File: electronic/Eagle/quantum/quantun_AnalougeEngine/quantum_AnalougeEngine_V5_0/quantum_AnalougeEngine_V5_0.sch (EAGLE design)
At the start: 204 parts, among them IC1 OP275, IC10 STM32F767ZIT6, IC11 AD7606BSTZ, IC2 DAC084S085CIMM_NOPB, IC3 DAC084S085CIMM_NOPB, IC4 OP275, IC5 OP275, IC6 LAN8742A-CZ-TR, IC7 TL072, IC8 OP275, IC9 TL072, J1 GWLEX-SMT-S988G_Y, K1 K1, K2 K2, K3 K3, K4 K4, K5 K5, K6 K6, K7 K7, K8 K8, T1 H1102NL, U12 ULN2003, U2 7812, U4 THAT1240, U6 THAT1240, U7 THAT1240, U8 THAT1240

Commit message: Continued on "AnlougeEngine_V_5_0" - Changed little timing in ADC read. Changed left/right send to FrontDisplay
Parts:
- removed CON1, CON2, CON3: (no value), electro_mechanical:PIN_HEADER_RIBBON_10_PIN_SMD
- removed R15, R16, R17, R18, R19, R20, R21, R22, R23, R24, R25, R26, R27: 10k, C_Sager_Bibliothek:RESISTOR
- added C44: 100nF, C_Sager_Bibliothek:CAPACITOR"
- added J2, J3, J4: 90814-0204, electro_mechanical:90814-0204
- added LED10, LED11, LED9: LED_BLUE_SMD, C_Sager_Bibliothek:LED_BLUE_SMD
- added R78: 10 k, C_Sager_Bibliothek:RESISTOR
- C41: value (none) -> 100 nF
- R13, R5: value 10k -> 680R; SPICEPREFIX R -> (none)
- R6: value 10k -> 680R
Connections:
- removed net N$10: IC11.V3, R16.2, R17.2
- removed net N$20: IC11.V5, R19.2, R24.2
- removed net N$35: IC11.V7, R21.2, R26.2
- removed net N$36: IC11.V8, R22.2, R27.2
- removed net N$46: R21.1
- new net DEBUG1: IC10.PF9
- new net DEBUG2: IC10.PD1
- new net LD1: IC10.PB0, LED9.+
- new net LD2: IC10.PB7, LED10.+
- new net LD3: IC10.PB14, LED11.+
- new net N$100: IC10.PC1
- new net N$101: IC10.PC2
- new net N$103: IC10.VDD_2
- new net N$104: IC10.VSSA
- new net N$105: IC10.VREF+
- new net N$106: IC10.VDDA
- new net N$107: IC10.PA0
- new net N$108: IC10.PA1
- new net N$109: IC10.PA2
- new net N$110: IC10.PA3
- new net N$111: IC10.VSS_2
- new net N$112: IC10.VDD_3
- new net N$115: IC10.PA6
- new net N$116: IC10.PA7
- new net N$117: IC10.PC4
- new net N$118: IC10.PC5
- new net N$120: IC10.PB1
- new net N$121: IC10.PB2
- new net N$122: IC10.PF11
- new net N$123: IC10.PF12
- new net N$124: IC10.VSS_3
- new net N$125: IC10.VDD_4
- new net N$126: IC10.PF13
- new net N$127: IC10.PF14
- new net N$128: IC10.PF15
- new net N$134: IC10.VSS_4
- new net N$135: IC10.VDD_5
- new net N$143: IC10.PB11
- new net N$144: IC10.VCAP_1
- new net N$145: IC10.VDD_6
- new net N$146: IC10.VDD_8
- new net N$147: IC10.VSS_7
- new net N$148: IC10.VCAP_2
- new net N$150: IC10.PA12
- new net N$151: IC10.PA11
- new net N$152: IC10.PA10
- new net N$153: IC10.PA9
- new net N$154: IC10.PA8
- new net N$159: IC10.VDDUSB
- new net N$160: IC10.VSS_6
- new net N$161: IC10.PG8
- new net N$162: IC10.PG7
- new net N$163: IC10.PG6
- new net N$164: IC10.PG5
- new net N$165: IC10.PG4
- new net N$168: IC10.PD15
- new net N$169: IC10.PD14
- new net N$170: IC10.VDD_7
- new net N$171: IC10.VSS_5
- new net N$172: IC10.PD13
- new net N$173: IC10.PD12
- new net N$174: IC10.PD11
- new net N$175: IC10.PD10
- new net N$178: IC10.PB15
- new net N$180: IC10.PB13
- new net N$181: IC10.PB12
- new net N$182: IC10.VDD_10
- new net N$183: IC10.PDR_ON
- new net N$186: IC10.PB9
- new net N$187: IC10.PB8
- new net N$188: IC10.BOOT0, R78.1
- new net N$190: IC10.PB6
- new net N$193: IC10.PB3
- new net N$195: IC10.VDD_9
- new net N$196: IC10.VSS_9
- new net N$197: IC10.PG14
- new net N$198: IC10.PG13
- new net N$200: IC10.PG11
- new net N$205: IC10.VDDSDMMC
- new net N$206: IC10.VSS_8
- new net N$207: IC10.PD5
- new net N$208: IC10.PD4
- new net N$209: IC10.PD3
- new net N$212: IC10.PD0
- new net N$216: IC10.PA15
- new net N$69: IC10.VBAT
- new net N$70: IC10.PC13
- new net N$76: IC10.PC14
- new net N$82: IC10.PC15
- new net N$83: IC10.PF0
- new net N$84: IC10.PF1
- new net N$85: IC10.PF2
- new net N$86: IC10.PF3
- new net N$87: IC10.PF4
- new net N$88: IC10.PF5
- new net N$89: IC10.VSS_1
- new net N$90: IC10.VDD_1
- new net N$91: IC10.PF6
- new net N$92: IC10.PF7
- new net N$93: IC10.PF8
- new net N$95: IC10.PF10
- new net N$96: IC10.PH0
- new net N$97: IC10.PH1
- new net N$99: IC10.PC0
- new net NRST: C44.2, IC10.NRST, J4.2, S1.3, S1.4
- new net SWCLK: IC10.PA14, J4.1
- new net SWDIO: IC10.PA13, J4.3
- new net USART3_RX: IC10.PD8
- new net USART3_TX: IC10.PD9
- new net USART6_RX: IC10.PC6
- new net USART6_TX: IC10.PC7
- net AGND: now also C44.1, J4.4, R13.1, R5.1, R78.2, S1.1, S1.2; no longer R15.1, R16.1, R23.1, R24.1, R25.1, R26.1, R27.1
- net BUSY: now also IC10.PG3
- net CS: now also IC10.PD7
- net CS_DAC1: now also IC10.PB4
- net CS_DAC2: now also IC10.PB5
- net CV_A_B: now also IC10.PC12
- net DAC_OUT1: now also IC10.PA4
- net DAC_OUT2: now also IC10.PA5
- net DB0: now also IC10.PE0
- net DB1: now also IC10.PE1
- net DB10: now also IC10.PE10
- net DB11: now also IC10.PE11
- net DB12: now also IC10.PE12
- net DB13: now also IC10.PE13
- net DB14: now also IC10.PE14
- net DB15: now also IC10.PE15
- net DB2: now also IC10.PE2
- net DB3: now also IC10.PE3
- net DB4: now also IC10.PE4
- net DB5: now also IC10.PE5
- net DB6: now also IC10.PE6
- net DB7: now also IC10.PE7
- net DB8: now also IC10.PE8
- net DB9: now also IC10.PE9
- net DIN_DAC: now also IC10.PC3
- net FRST: now also IC10.PD6
- net L/M_IN(VCA1_IN): now also IC11.V1; no longer R5.1
- net L/M_OUT(OUT_STAGE_LEFT): now also IC11.V5; no longer R19.1
- net L/M_OUT(VCA1_OUT): now also IC11.V3; no longer R17.1
- net N$12: now also LED10.-, R6.2; no longer IC11.V4, R18.2, R23.2
- net N$34: now also LED11.-, R13.2; no longer IC11.V6, R20.2, R25.2
- net N$4: now also IC11.V7; no longer IC11.V1, R5.2, R6.2
- net N$47: now also IC11.V8; no longer R22.1
- net N$6: now also LED9.-, R5.2; no longer IC11.V2, R13.2, R15.2
- net OS0: now also IC10.PC8
- net OS1: now also IC10.PC9
- net OS2: now also IC10.PC10
- net R/S_IN(VCA2_IN): now also IC11.V2; no longer R13.1
- net R/S_OUT(OUT_STAGE_RIGHT): now also IC11.V6; no longer R20.1
- net R/S_OUT(VCA2_OUT): now also IC11.V4; no longer R18.1
- net RANGE: now also IC10.PC11
- net RD: now also IC10.PD2
- net RELAIS1: now also IC10.PG1
- net RELAIS2: now also IC10.PG0
- net RELAIS3: now also IC10.PG15
- net RELAIS4: now also IC10.PG10
- net RELAIS5: now also IC10.PG12
- net RELAIS6: now also IC10.PG9
- net RESET: now also IC10.PG2
- net SCLK_DAC: now also IC10.PB10
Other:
- note added: "debug LEDs"
- note added: "operational voltage"
- note added: "prg.adapter"
- note added: "reset switch"

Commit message: progess on Analouge Engine V_5_0
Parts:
- removed C69: 0.33 uF, C_Sager_Bibliothek:CAPACITOR"
- removed C70: 100 nF, C_Sager_Bibliothek:CAPACITOR"
- removed J2, J3, J4: 90814-0204, electro_mechanical:90814-0204
- removed R77: 0R, C_Sager_Bibliothek:RESISTOR
- removed TP03, TP05, TP06: TPTHT, C_Sager_Bibliothek:TPTHT
- removed U2: 7812, C_Sager_Bibliothek:78
- added ANALOGVOLT, DIG_VOLT, PROG.: 90814-0204, electro_mechanical:90814-0204
- added DEBUG1, DEBUG2, TP04: TPTHT, C_Sager_Bibliothek:TPTHT
- added IC12: ESDA6V1BC6, NUCLEO_parts:ESDA6V1BC6
- added R15, R16, R17: 0R, C_Sager_Bibliothek:RESISTOR
- added R18, R19: 10 k, C_Sager_Bibliothek:RESISTOR
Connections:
- net N$100 renamed RMII_MDC
- net N$108 renamed RMII_REF_CLK
- net N$109 renamed RMII_MDIO
- net N$116 renamed RMSII_CRS_DV
- net N$117 renamed RMII_RXD0
- net N$118 renamed RMII_RXD1
- net N$15 renamed NEGATIVE_OUT(L/M)
- net N$152 renamed USB_ID
- net N$17 renamed POSITIVE_OUT(L/M)
- net N$180 renamed RMII_TXD1
- net N$188 renamed BOOT0
- net N$198 renamed RMII_TXD0
- net N$200 renamed RMII_TX_EN
- net N$21 renamed POSITIVE_IN(R/S)
- net N$22 renamed NEGATIVE_IN(R/S)
- net N$23 renamed POSITIVE_OUT(R/S)
- net N$24 renamed NGATIVE_OUT(R/S)
- net N$25 renamed NEGATIVE_IN(L/M)
- net N$27 renamed POSITIVE_IN(L/M)
- removed net +5V_STM32: C19.1, C31.1, C33.1, C43.1, IC2.VA, IC3.VA
- removed net BOTTOM: TP06.TP
- removed net N$101: IC10.PC2
- removed net N$103: IC10.VDD_2
- removed net N$104: IC10.VSSA
- removed net N$105: IC10.VREF+
- removed net N$106: IC10.VDDA
- removed net N$107: IC10.PA0
- removed net N$110: IC10.PA3
- removed net N$111: IC10.VSS_2
- removed net N$112: IC10.VDD_3
- removed net N$115: IC10.PA6
- removed net N$120: IC10.PB1
- removed net N$121: IC10.PB2
- removed net N$122: IC10.PF11
- removed net N$123: IC10.PF12
- removed net N$124: IC10.VSS_3
- removed net N$125: IC10.VDD_4
- removed net N$126: IC10.PF13
- removed net N$127: IC10.PF14
- removed net N$128: IC10.PF15
- removed net N$134: IC10.VSS_4
- removed net N$135: IC10.VDD_5
- removed net N$143: IC10.PB11
- removed net N$144: IC10.VCAP_1
- removed net N$145: IC10.VDD_6
- removed net N$146: IC10.VDD_8
- removed net N$147: IC10.VSS_7
- removed net N$148: IC10.VCAP_2
- removed net N$150: IC10.PA12
- removed net N$151: IC10.PA11
- removed net N$153: IC10.PA9
- removed net N$154: IC10.PA8
- removed net N$159: IC10.VDDUSB
- removed net N$160: IC10.VSS_6
- removed net N$161: IC10.PG8
- removed net N$162: IC10.PG7
- removed net N$163: IC10.PG6
- removed net N$164: IC10.PG5
- removed net N$165: IC10.PG4
- removed net N$168: IC10.PD15
- removed net N$169: IC10.PD14
- removed net N$170: IC10.VDD_7
- removed net N$171: IC10.VSS_5
- removed net N$172: IC10.PD13
- removed net N$173: IC10.PD12
- removed net N$174: IC10.PD11
- removed net N$175: IC10.PD10
- removed net N$178: IC10.PB15
- removed net N$181: IC10.PB12
- removed net N$182: IC10.VDD_10
- removed net N$183: IC10.PDR_ON
- removed net N$186: IC10.PB9
- removed net N$187: IC10.PB8
- removed net N$190: IC10.PB6
- removed net N$193: IC10.PB3
- removed net N$195: IC10.VDD_9
- removed net N$196: IC10.VSS_9
- removed net N$197: IC10.PG14
- removed net N$205: IC10.VDDSDMMC
- removed net N$206: IC10.VSS_8
- removed net N$207: IC10.PD5
- removed net N$208: IC10.PD4
- removed net N$209: IC10.PD3
- removed net N$212: IC10.PD0
- removed net N$37: R77.2, TP05.TP
- removed net N$69: IC10.VBAT
- removed net N$70: IC10.PC13
- removed net N$76: IC10.PC14
- removed net N$82: IC10.PC15
- removed net N$83: IC10.PF0
- removed net N$84: IC10.PF1
- removed net N$85: IC10.PF2
- removed net N$86: IC10.PF3
- removed net N$87: IC10.PF4
- removed net N$88: IC10.PF5
- removed net N$89: IC10.VSS_1
- removed net N$90: IC10.VDD_1
- removed net N$91: IC10.PF6
- removed net N$92: IC10.PF7
- removed net N$93: IC10.PF8
- removed net N$95: IC10.PF10
- removed net N$96: IC10.PH0
- removed net N$97: IC10.PH1
- removed net N$99: IC10.PC0
- new net +3V3: ANALOGVOLT.1
- new net +5V: ANALOGVOLT.4, C19.1, C31.1, C33.1, C41.1, C43.1, IC11.AVCC_1, IC11.AVCC_2, IC11.AVCC_3, IC11.AVCC_4, IC11.VDRIVE, IC2.VA, IC3.VA, R29.2, R35.1
- new net A_GND_TO_STAR: DIG_VOLT.3, R16.1
- new net D_GND_TO_STAR: ANALOGVOLT.3, R15.1
- new net N$10: IC10.PA9, R19.1
- new net PB2/BOOT1: IC10.PB2, R18.2
- new net USB_DM: IC10.PA11, IC12.3, X1.2
- new net USB_DP: IC10.PA12, IC12.6, X1.3
- new net USB_VBUS: IC12.1, R19.2, X1.1
- net +12V: now also ANALOGVOLT.2; no longer C70.1, U2.VO
- net +5V_DIGITAL: no longer C41.1, IC11.AVCC_2, IC11.AVCC_3, IC11.AVCC_4, IC11.VDRIVE, R29.2, R35.1
- net AGND: now also IC11.AGND_1, IC12.2, IC12.5, PROG..4, R15.2, R16.2, R17.2, R18.1, X1.4; no longer C69.2, C70.2, J4.4, U2.GND
- net CHASIS: now also R17.1, TP04.TP; no longer R77.1, TP03.TP
- net DEBUG1: now also DEBUG1.TP
- net DEBUG2: now also DEBUG2.TP
- net L/M_OUT+: now also K33.S; no longer K32.S
- net L/M_OUT-: now also K32.S; no longer K33.S
- net NRST: now also PROG..2; no longer J4.2
- net R/S_OUT+: now also K23.S; no longer K22.S
- net R/S_OUT-: now also K22.S; no longer K23.S
- net SWCLK: now also PROG..1; no longer J4.1
- net SWDIO: now also PROG..3; no longer J4.3
- net V+: now also DIG_VOLT.1; no longer C69.1, U2.VI
- net V-: now also DIG_VOLT.2
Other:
- note added: "1 Ground/Shield 2 Positive 3 Negative"
- note added: "1646 gives +6 dB amplification by default."
- note added: "Chassis"
- note added: "GND StarPoint"
- note added: "INFO:"
- note added: "M/S <->normal"
- note added: "Main Controller"
- note added: "USB port"
- note added: "Voltages"
- note added: "XLR"
- note added: "analog voltage IN"
- note added: "digital voltage IN"
- note added: "protocol slect"
- note removed: "Analog Voltage"
- note removed: "Attention SPI is not configured jet in CubeMX"
- note removed: "Digital Voltage"
- note removed: "StarPoint"
- note removed: "use: SPI2: Transmit Only Master PB10: SPI2_SCK PC3: SPI2_MOSI PB4: CS_DAC1 PB5: CS_DAC2"

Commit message: progress Analog Engine V_5_0
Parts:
- removed ANALOGVOLT, DIG_VOLT: 90814-0204, electro_mechanical:90814-0204
- added +12V_OK, +15V_OK, +3V3_OK, +5V_OK, -15V_OK: LED_GREEN_SMD, passive components:LED_GREEN_SMD
- added ANALOG_VOLT, DIGITAL_VOLT, DISPLAY: 90814-0204, electro_mechanical:90814-0204
- added C100: 30 pF, passive components:CAPACITOR_0603
- added C101: 4.7 uF, passive components:CAPACITOR_1206
- added C102, C91, C99: 10 uF, passive components:CAPACITOR_1206
- added C103, C95, C96, C97, C98: 100nF, C_Sager_Bibliothek:CAPACITOR"
- added C65, C66: 2.7 pF, passive components:CAPACITOR_0603
- added C69, C70: 4.3 pF, passive components:CAPACITOR_0603
- added C71, C72: 2.2 uF, passive components:CAPACITOR_1206
- added C73, C74, C75, C76, C77, C78, C79, C80, C81, C82, C83, C84, C85, C86, C87, C90, C92, C93, C94: 100 nF, passive components:CAPACITOR_0603
- added C88: 1 uF, passive components:CAPACITOR_0603
- added C89: 470 pF, passive components:CAPACITOR_0603
- added IC13: USBLC6-4SC6, NUCLEO_parts:USBLC6-4SC6
- added IC14, IC15: TL072, C_Sager_Bibliothek:TL072
- added IC16: OP275, C_Sager_Bibliothek:OP275
- added R100: 150 R, C_Sager_Bibliothek:RESISTOR
- added R101: 500 R, C_Sager_Bibliothek:RESISTOR
- added R20, R21, R23, R27, R85: 10 k, C_Sager_Bibliothek:RESISTOR
- added R22: 1k5, C_Sager_Bibliothek:RESISTOR
- added R24, R25, R26: 33 R, C_Sager_Bibliothek:RESISTOR
- added R77: 12k1, C_Sager_Bibliothek:RESISTOR
- added R79, R80, R81, R82: 50 R, C_Sager_Bibliothek:RESISTOR
- added R83, R84: 270 R, C_Sager_Bibliothek:RESISTOR
- added R86: 100k, C_Sager_Bibliothek:RESISTOR
- added R87: 10k, C_Sager_Bibliothek:RESISTOR
- added R88, R89, R90: 75 R, C_Sager_Bibliothek:RESISTOR
- added R91: 0 R, C_Sager_Bibliothek:RESISTOR
- added R97, R98: 650 R, C_Sager_Bibliothek:RESISTOR
- added R99: 65 R, C_Sager_Bibliothek:RESISTOR
- added Y1: NX3215SA-32.768K-STD-MUA-8, NUCLEO_parts:NX3215SA-32.768K-STD-MUA-8
- added Y2: NX3225GD-8MHZ-STD-CRA-3, NUCLEO_parts:NX3225GD-8MHZ-STD-CRA-3
- added Y3: ABLS2-25.000MHZ-D4YF-T, NUCLEO_parts:ABLS2-25.000MHZ-D4YF-T
- C39: value 10 µF -> 10 uF; device C_Sager_Bibliothek:ELECTROLYTICELCTROLYTIC_MIDSIZE_SMD -> passive components:CAPACITOR_1206
- C40: value 10 µF -> 30 pF; device C_Sager_Bibliothek:ELECTROLYTICELCTROLYTIC_MIDSIZE_SMD -> passive components:CAPACITOR_0603
- C67: value 47µF -> 10 uF; device C_Sager_Bibliothek:ELECTROLYTICELCTROLYTIC_MIDSIZE_SMD -> passive components:CAPACITOR_1206
- C68: value 47µF -> 100nF; device C_Sager_Bibliothek:ELECTROLYTICELCTROLYTIC_MIDSIZE_SMD -> C_Sager_Bibliothek:CAPACITOR"
- R29: value 10k -> 75 R
- R38, R41, R44, R64: value 51k -> 27k
- R39, R45: value 51R -> 100k; SPICEPREFIX (none) -> R
- R40, R43, R63, R66: value 90k9 -> 160 k
- R42, R65: value 51R -> 10k
- renumbered LED10 to LD2, LED11 to LD3, LED9 to LD1
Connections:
- net USB_DM renamed USB_N
- net USB_DP renamed USB_P
- removed net +5V_DIGITAL: R1.2
- removed net ADC1-IN0: R3.1, R4.2
- removed net ADC1-IN3: R1.1, R2.2
- removed net DGND: C19.2, C31.2, C33.2, C43.2, IC2.GND, IC3.GND
- removed net N$216: IC10.PA15
- removed net PB2/BOOT1: IC10.PB2, R18.2
- removed net RMSII_CRS_DV: IC10.PA7
- new net +12V_SIG: IC10.PA6, R39.1, R42.2
- new net +15V_SIG: IC10.PA0, R3.1, R4.2
- new net +3V3_SIG: IC10.PB1, R45.1, R65.2
- new net +5V_SIG: IC10.PC0, R86.1, R87.2
- new net -15V_SIG: IC10.PA3, R1.1, R2.2
- new net 1V_DAC_UNBUFFERD: C20.1, C64.1, IC15G$2.+IN, R61.2, R68.1, R69.2
- new net 32.768KHZ_A: C66.1, IC10.PC14, Y1.1
- new net 32.768KHZ_B: C65.1, IC10.PC15, Y1.2
- new net 8MHZ_CRYSTAL_A: C70.1, IC10.PH0, Y2.1
- new net 8MHZ_CRYSTAL_B: C69.1, IC10.PH1, Y2.2
- new net LED1: IC6.LED1/NINT/NPME/!REGOFF, J1.YELLOW_A, R85.2
- new net LED2: IC6.LED2/NINT/NPME/!NINTSEL, J1.GREEN_A
- new net N$15: C71.1, IC10.VCAP_1
- new net N$17: C72.1, IC10.VCAP_2
- new net N$20: C80.2, IC10.VDDA, IC10.VREF+
- new net N$21: IC6.RXD1/!MODE1, R18.2, R24.2
- new net N$22: IC6.RXD0/!MODE0, R20.2, R25.2
- new net N$23: IC6.CRS_DV/!MODE2, R21.2, R26.2
- new net N$24: IC6.RXER/!PHYAD0, R27.2
- new net N$25: IC6.RBIAS, R77.1
- new net N$27: C88.2, C89.2, IC6.VDDCR
- new net N$35: J1.1, T1.TX+
- new net N$36: J1.2, T1.TX-
- new net N$37: J1.3, T1.RX+
- new net N$46: J1.6, T1.RX-
- new net N$50: J1.GREEN_K, R84.2
- new net N$52: J1.YELLOW_K, R83.2
- new net N$62: IC7G$2.+IN, R46.2, R73.1
- new net N$66: IC14G$2.+IN, R58.2, R59.1
- new net N$67: IC15G$1.+IN, R60.2, R61.1
- new net N$69: C40.2, IC6.XTAL2, Y3.1
- new net N$70: C100.2, IC6.XTAL1/CLKIN, Y3.2
- new net N$76: -15V_OK.+, R97.2
- new net N$82: +15V_OK.+, R98.1
- new net N$83: +3V3_OK.+, R99.1
- new net N$84: +5V_OK.+, R100.1
- new net N$85: +12V_OK.+, R101.1
- new net N$86: J1.7, R29.2
- new net N$87: J1.8, R88.2
- new net N$88: R89.2, T1.NC_4
- new net N$89: R90.2, T1.NC_6
- new net N$90: C101.1, R29.1, R88.1, R89.1, R90.1
- new net N$92: C101.2, J1.13, J1.14, R91.2
- new net RD_N: IC13.I/O4, IC6.RXN, R82.1, T1.RD-
- new net RD_P: IC13.I/O1, IC6.RXP, R81.1, T1.RD+
- new net RMII_CRS_DV: IC10.PA7, R26.1
- new net TD_N: IC13.I/O3, IC6.TXN, R80.1, T1.TD-
- new net TD_P: IC13.I/O2, IC6.TXP, R79.1, T1.TD+
- new net USB_OVERCURRENT: IC10.PG7
- new net USB_POWERSWITCHON: IC10.PG6
- new net USB_SOF: IC10.PA8
- net +12V: now also DIGITAL_VOLT.2, DISPLAY.3, R101.2, R39.2; no longer ANALOGVOLT.2
- net +3V3: now also C73.1, C74.1, C75.1, C76.1, C77.1, C78.1, C79.1, C81.2, C82.2, C83.1, C84.1, C85.1, C86.2, C87.2, C90.2, C91.1, C92.2, C93.2, C94.2, DIGITAL_VOLT.1, IC10.VBAT, IC10.VDDSDMMC, IC10.VDDUSB, IC10.VDD_1, IC10.VDD_10, IC10.VDD_2, IC10.VDD_3, IC10.VDD_4, IC10.VDD_5, IC10.VDD_6, IC10.VDD_7, IC10.VDD_8, IC10.VDD_9, IC13.VBUS, IC6.VDD1A, IC6.VDD2A, IC6.VDDIO, R18.1, R20.1, R21.1, R22.1, R23.2, R45.2, R79.2, R80.2, R81.2, R82.2, R99.2, T1.CT_1, T1.CT_2; no longer ANALOGVOLT.1
- net +5V: now also C24.1, C34.1, DIGITAL_VOLT.4, IC2.VREFIN, R1.2, R100.2, R86.2; no longer ANALOGVOLT.4, R29.2
- net .: now also IC14G$1.OUT; no longer IC7G$2.OUT
- net 0,5V_DAC: now also IC14G$1.+IN, IC15G$1.-IN, IC15G$1.OUT; no longer IC7G$2.+IN, R60.2, R61.1
- net 1V_DAC: now also IC15G$2.-IN, IC15G$2.OUT; no longer C20.1, C24.1, C34.1, C64.1, IC2.VREFIN, R61.2, R68.1, R69.2
- net AGND: now also +12V_OK.-, +15V_OK.-, +3V3_OK.-, +5V_OK.-, -15V_OK.-, C100.1, C103.2, C19.2, C31.2, C33.2, C39.2, C40.1, C43.2, C65.2, C66.2, C68.2, C69.2, C70.2, C71.2, C72.2, C73.2, C74.2, C75.2, C76.2, C77.2, C78.2, C79.2, C80.1, C81.1, C82.1, C83.2, C84.2, C85.2, C86.1, C87.1, C88.1, C89.1, C90.1, C91.2, C92.1, C93.1, C94.1, C95.2, C96.2, C97.2, C98.2, C99.2, DISPLAY.4, IC10.VSSA, IC10.VSS_1, IC10.VSS_2, IC10.VSS_3, IC10.VSS_4, IC10.VSS_5, IC10.VSS_6, IC10.VSS_7, IC10.VSS_8, IC10.VSS_9, IC13.GND, IC2.GND, IC3.GND, IC6.EP_VSS, R27.1, R77.2, R83.1, R84.1, R85.1, R87.1; no longer C39.-, C40.-, R18.1, R39.1, R45.1
- net A_GND_TO_STAR: now also ANALOG_VOLT.3; no longer DIG_VOLT.3
- net CHASIS: now also R91.1
- net DAC2_OUT1(OFFSET_VCA1): now also C99.1; no longer C39.+
- net DAC2_OUT2(OFFSET_VCA2): now also C39.1; no longer C40.+
- net D_GND_TO_STAR: now also DIGITAL_VOLT.3; no longer ANALOGVOLT.3
- net E+_OUT_STAGE_LEFT: now also IC7G$2.-IN, IC7G$2.OUT; no longer R46.2, R73.1
- net E+_OUT_STAGE_RIGHT: now also IC14G$2.-IN, IC14G$2.OUT; no longer R58.2, R59.1
- net L/M_IN(VCA1_IN): now also C102.1; no longer C67.+
- net N$18: now also U6.IN+; no longer U6.IN-
- net N$33: now also IC16A.-IN, IC16A.OUT, U6.IN-; no longer IC4B.-IN, IC4B.OUT, U6.IN+
- net N$38: no longer R29.1
- net N$43: now also U8.IN-; no longer U8.IN+
- net N$45: now also U8.IN+; no longer U8.IN-
- net N$71: now also C102.2; no longer C67.-
- net N$74: now also IC14G$1.-IN; no longer IC7G$2.-IN
- net N$78: now also C67.2; no longer C68.-
- net NRST: now also IC6.NRST
- net R: now also IC16A.+IN; no longer IC4B.+IN
- net R/S_IN(VCA2_IN): now also C67.1; no longer C68.+
- net RMII_MDC: now also IC6.MDC
- net RMII_MDIO: now also IC6.MDIO, R22.2
- net RMII_REF_CLK: now also IC6.NINT/REFCLKO, R23.1
- net RMII_RXD0: now also R25.1
- net RMII_RXD1: now also R24.1
- net RMII_TXD0: now also IC6.TXD0
- net RMII_TXD1: now also IC6.TXD1
- net RMII_TX_EN: now also IC6.TXEN
- net SYM1: no longer R39.2
- net SYM2: no longer R42.2
- net SYM3: no longer R45.2
- net SYM4: no longer R65.2
- net USART6_RX: now also DISPLAY.2, IC10.PC7; no longer IC10.PC6
- net USART6_TX: now also DISPLAY.1, IC10.PC6; no longer IC10.PC7
- net V+: now also ANALOG_VOLT.1, C68.1, C95.1, C97.1, IC14G$3.V+, IC15G$3.V+, IC16P.V+, R98.2; no longer DIG_VOLT.1
- net V-: now also ANALOG_VOLT.2, C103.1, C96.1, C98.1, IC14G$3.V-, IC15G$3.V-, IC16P.V-, R97.1; no longer DIG_VOLT.2
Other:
- note added: "32.768 kHz"
- note added: "8 MHZ"
- note added: "ADC1_IN0"
- note added: "ADC1_IN10"
- note added: "ADC1_IN3"
- note added: "ADC1_IN6"
- note added: "ADC1_IN9"
- note added: "DAC Ref Voltages"
- note added: "Ethernet PHY"
- note added: "Output Gain Control"
- note added: "SYM THD VCAs"
- note added: "Signal Conditioning"
- note added: "Voltage control LEDs"
- note added: "diff pair"
- note added: "main VCA offset"
- note removed: "high=serial low=parallel"
- note removed: "measure negative supply voltage"
- note removed: "measure positive supply voltage"
- note removed: "operational voltage"
- note removed: "protocol slect"
- moved on the sheet: C19, C20, C23, C24, C31, C32, C33, C34, C41, C42, C43, C49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

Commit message: placement of components done AnalougeEngine V5_0
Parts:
- added R92, R93, R94, R95: 500 R, C_Sager_Bibliothek:RESISTOR
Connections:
- new net N$91: IC2.SCLK, IC3.SCLK, R92.1
- new net N$93: IC2.DIN, IC3.DIN, R93.1
- new net N$94: IC2.!SYNC, R94.1
- new net N$95: IC3.!SYNC, R95.1
- net CS_DAC1: now also R94.2; no longer IC2.!SYNC
- net CS_DAC2: now also R95.2; no longer IC3.!SYNC
- net DIN_DAC: now also R93.2; no longer IC2.DIN, IC3.DIN
- net SCLK_DAC: now also R92.2; no longer IC2.SCLK, IC3.SCLK
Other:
- moved on the sheet: C23, C24, C39, C49, C50, C95, C96, C99, R47, R76

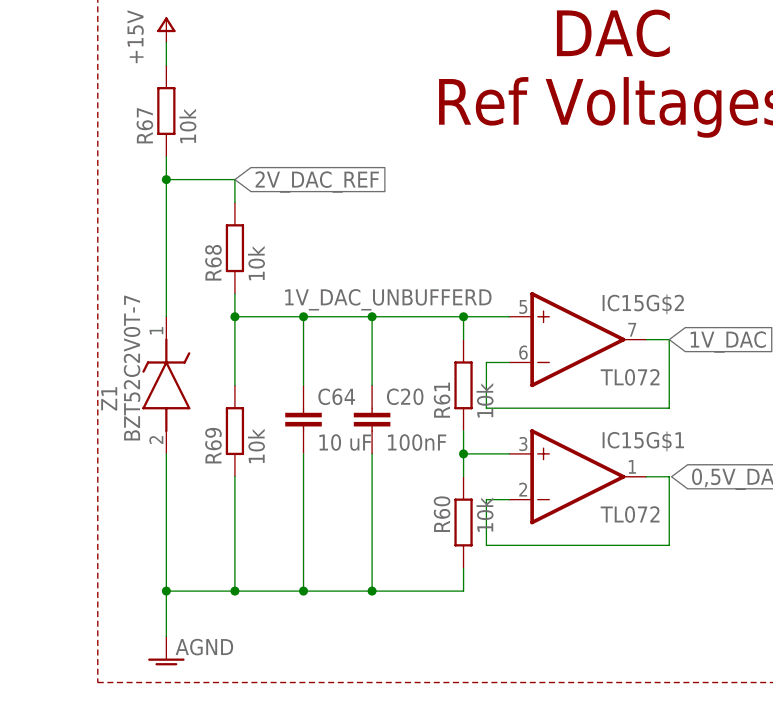
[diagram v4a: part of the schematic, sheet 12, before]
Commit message: Clock changed to 8 MHz Crystal. Progress AnalougeEngine (routing 50 %).
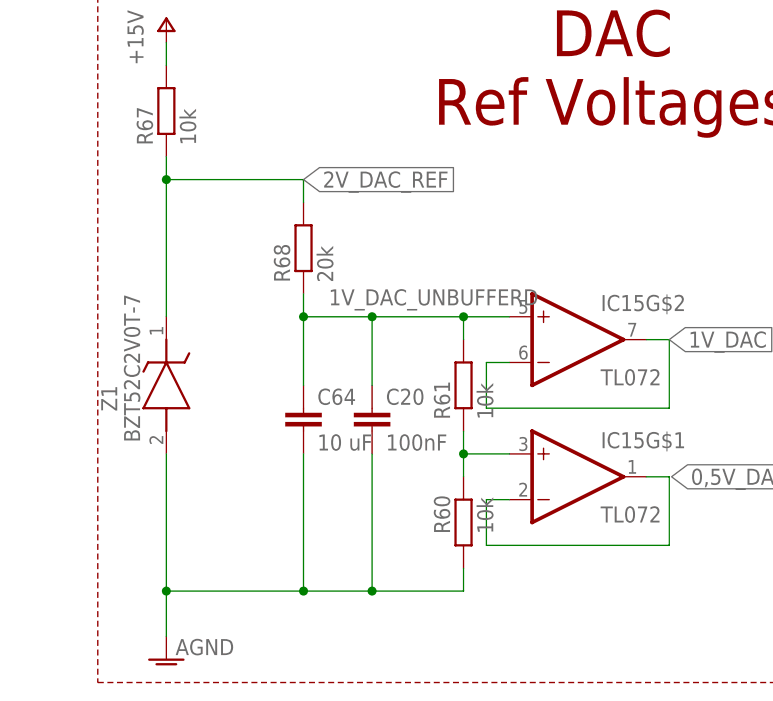
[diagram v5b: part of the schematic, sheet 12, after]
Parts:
- removed TP04: TPTHT, C_Sager_Bibliothek:TPTHT
- R68: value 10k -> 20k
- R69: value 10k -> 0R
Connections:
- new net DISPLAY_GND_TO_STAR: DISPLAY.4, R69.1
- net +12V: no longer DISPLAY.3
- net +5V: now also DISPLAY.3
- net 1V_DAC_UNBUFFERD: no longer R69.2
- net AGND: now also R69.2; no longer DISPLAY.4, R69.1
- net A_GND_TO_STAR: now also ANALOG_VOLT.4
- net CHASIS: now also X1.P$1, X1.P$2; no longer TP04.TP
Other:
- note added: "display adapter"
- moved on the sheet: DEBUG1, DEBUG2, R68
